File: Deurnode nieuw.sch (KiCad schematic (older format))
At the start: 40 parts, among them J1 EXT1, J10 Jumper Output, J11 Jumper Rel./Fet, J12 Screw_Terminal_01x03, J13 Screw_Terminal_01x03, J14 Screw_Terminal_01x02, J15 Screw_Terminal_01x02, J16 Conn_01x02, J17 Conn_01x02, J18 Barrel_Jack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

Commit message: By means of two jumpers the FET components are isolated from the rest of the board. Current concept version 0.5
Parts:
- removed J13: Screw_Terminal_01x03, TerminalBlock_RND:TerminalBlock_RND_205-00288_1x03_P5.08mm_Horizontal, symbol Connector:Screw_Terminal_01x03
- added J13: Jumper 2 External Power, Connector_PinHeader_2.54mm:PinHeader_1x02_P2.54mm_Vertical, symbol Connector_Generic:Conn_01x02
- added J20: Jumper 1 External Power, Connector_PinHeader_2.54mm:PinHeader_1x03_P2.54mm_Vertical, symbol Connector_Generic:Conn_01x03
- added J21: Screw_Terminal_01x04, TerminalBlock_RND:TerminalBlock_RND_205-00289_1x04_P5.08mm_Horizontal, symbol Connector:Screw_Terminal_01x04
- added OK3: PC814, PC814:DIL04, symbol PC814:PC814
- added R11: 47k, Resistor_THT:R_Axial_DIN0207_L6.3mm_D2.5mm_P7.62mm_Horizontal, symbol Device:R
- R4: value 2k2 -> 4k7
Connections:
- net +12V: now also J20.1 (Pin_1); no longer D2.1 (K)
- net GND: now also J13.1 (Pin_1); no longer D3.1 (K), R5.2, U1.3 (S)
- net at D2.2 (A), R10.1, U1.2 (D): now also J21.3 (Pin_3)
- net at R5.1, U1.1 (G): now also OK3.3 (E); no longer J11.3 (Pin_3)
- net at J10.3 (Pin_3), J11.2 (Pin_2): no longer R4.2
- new net: D2.1 (K), J20.2 (Pin_2), J21.2 (Pin_2), R11.1
- new net: D3.1 (K), J13.2 (Pin_2), J21.4 (Pin_4), R5.2, U1.3 (S)
- new net: J20.3 (Pin_3), J21.1 (Pin_1)
- new net: J11.3 (Pin_3), OK3.1 (AC1)
- new net: OK3.2 (AC2), R4.2
- new net: OK3.4 (C), R11.2
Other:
- note added: "+12V"
- note added: "1A"
- note added: "1B"
- note added: "2A"
- note added: "2B"
- note added: "Coil +"
- note added: "Coil -"
- note added: "Common"
- note added: "Default 230V AC"
- note added: "Ext. gnd"
- note added: "Ext. power +"
- note added: "GND"
- note added: "NC"
- note added: "NO"
- note added: "Schakelaar"
- note removed: "Grote schakelaar"
- moved on the sheet: D1, D2, J10, J11, J12, J4, J5, K1, R2, R5

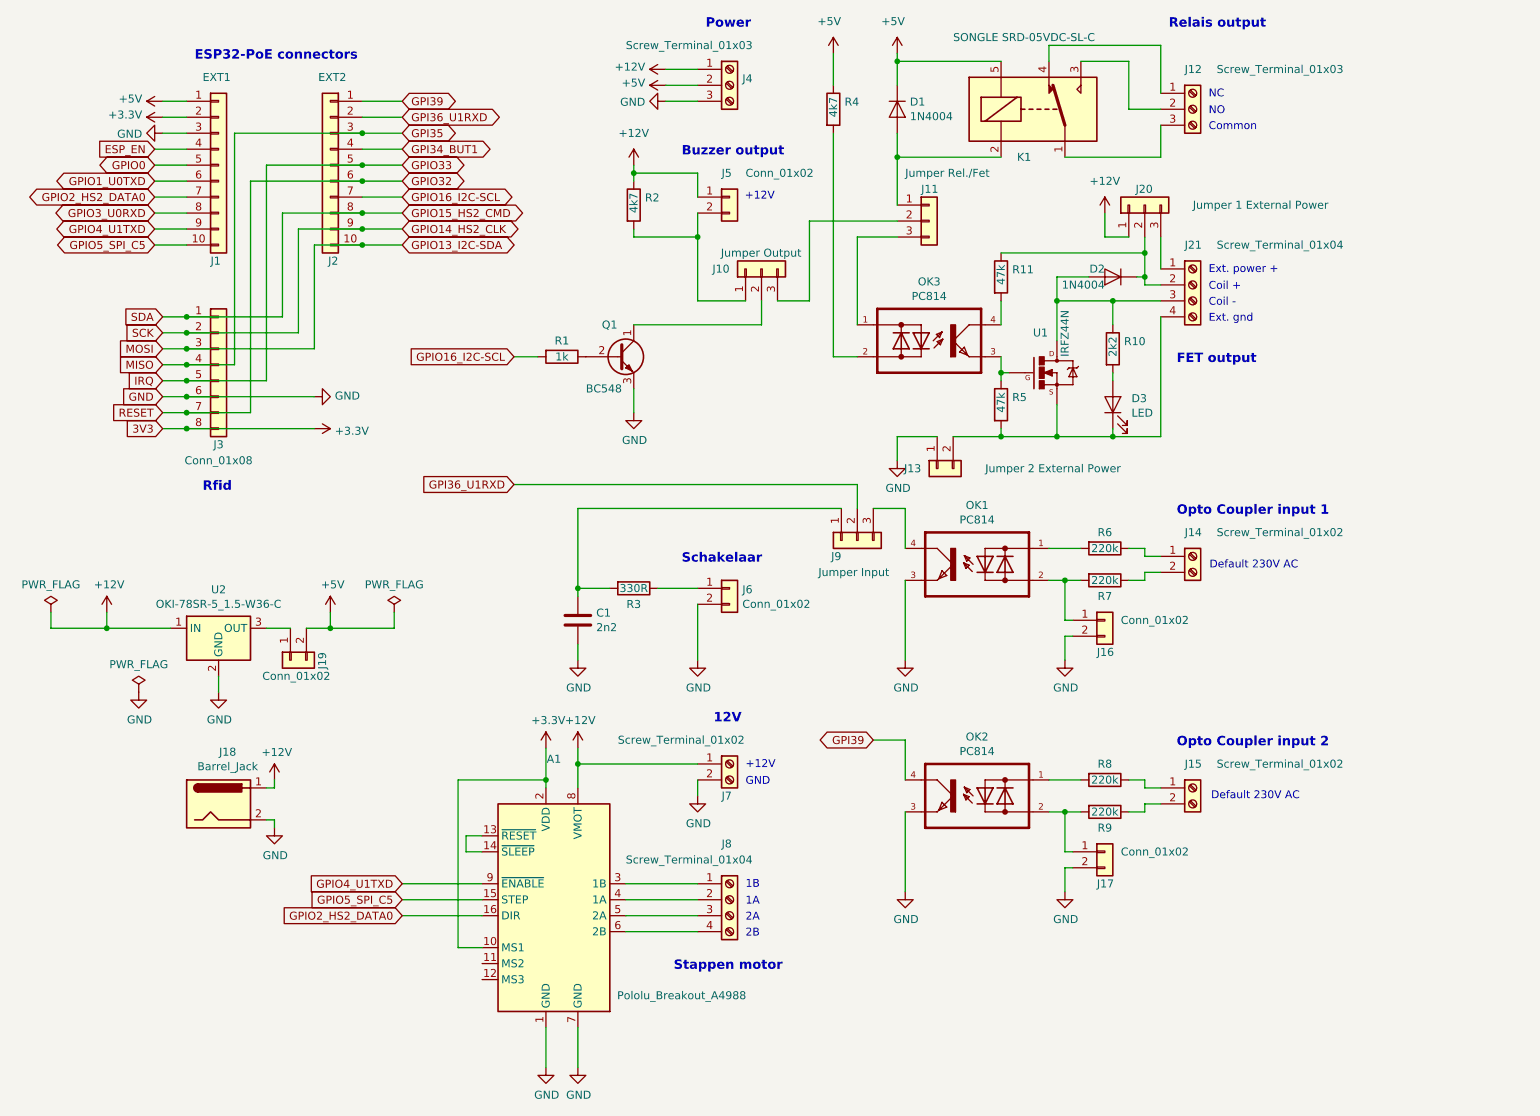
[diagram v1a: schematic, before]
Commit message: Jumper added for Relais/FET override + correct footprint made for 12V barel jack current version concept V0.6
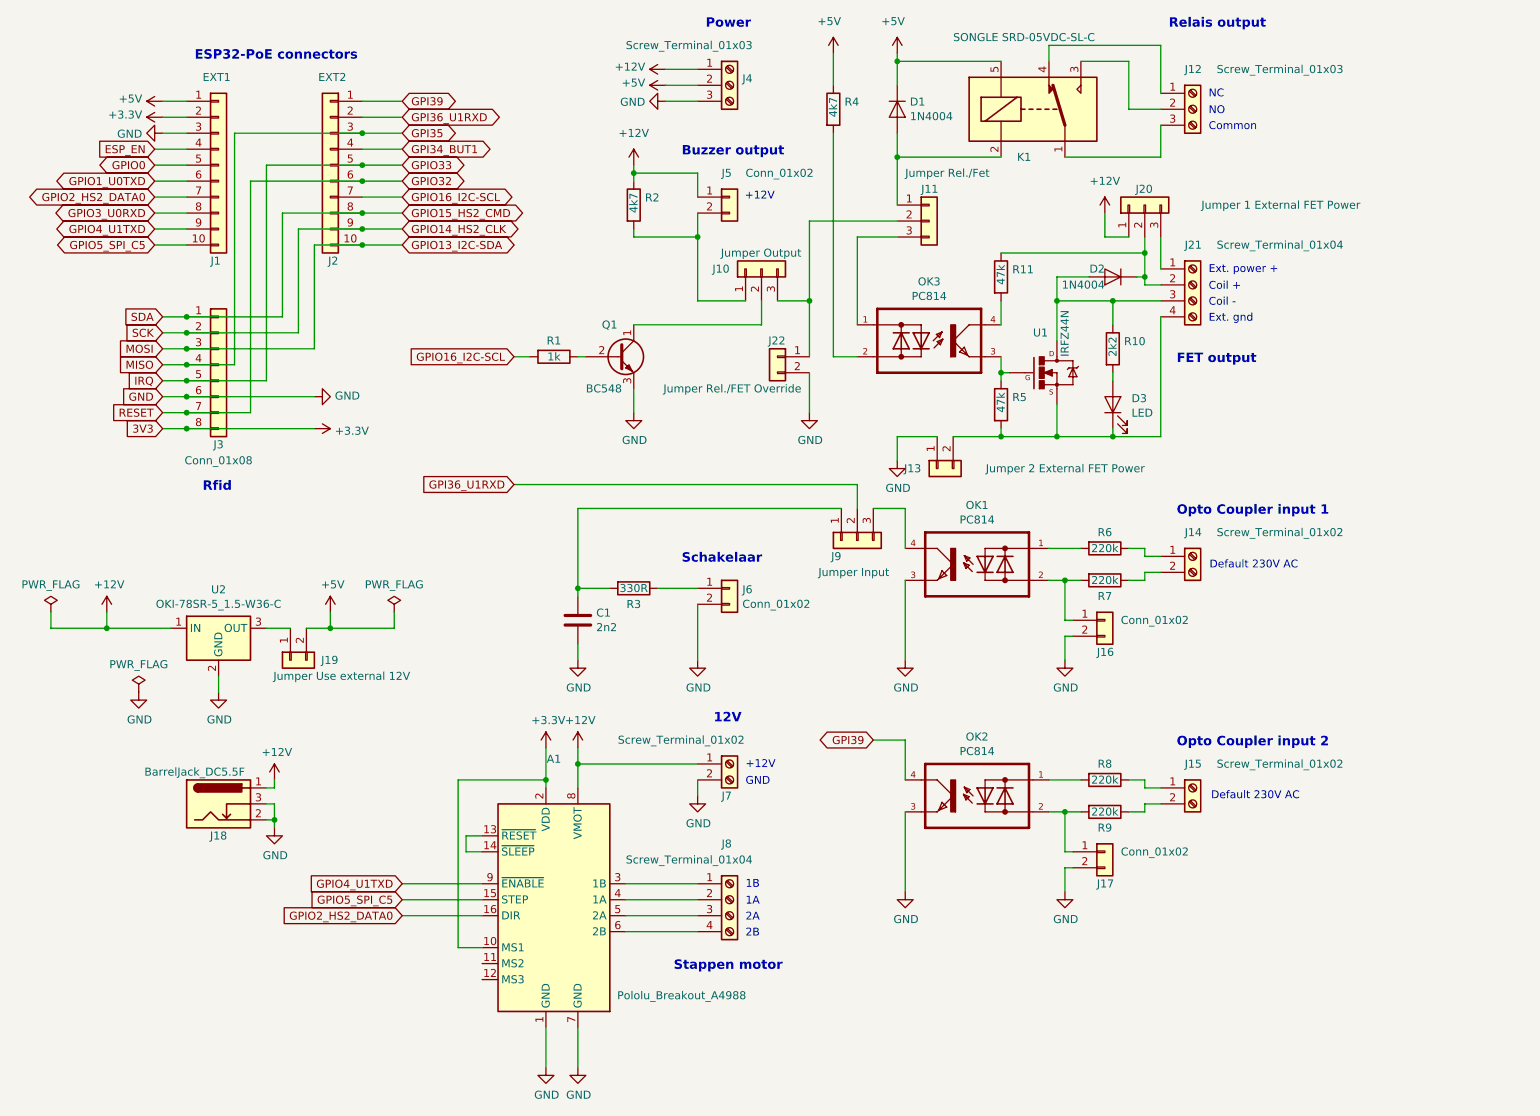
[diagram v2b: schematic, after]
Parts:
- removed J18: Barrel_Jack, Connector_BarrelJack:BarrelJack_CUI_PJ-063AH_Horizontal_CircularHoles, symbol Connector:Barrel_Jack
- added J18: BarrelJack_DC5.5F, Footprints:BarrelJack_DC5.5F, symbol Connector:Barrel_Jack_Switch
- added J22: Jumper Rel./FET Override, Connector_PinHeader_2.54mm:PinHeader_1x02_P2.54mm_Vertical, symbol Connector_Generic:Conn_01x02
- J13: value Jumper 2 External Power -> Jumper 2 External FET Power
- J19: value Conn_01x02 -> Jumper Use external 12V
- J20: value Jumper 1 External Power -> Jumper 1 External FET Power
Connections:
- net +12V: now also J18.1
- net GND: now also J18.2, J18.3, J22.2 (Pin_2)
- net at J10.3 (Pin_3), J11.2 (Pin_2): now also J22.1 (Pin_1)
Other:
- moved on the sheet: R1
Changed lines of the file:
@@
 Sheet 1 1
 Title "Deurnode (based on Olimex ESP32-POE)"
-Date "2020-03-03"
-Rev "Version 0.5"
+Date "2020-03-05"
+Rev "Version 0.6"
 Comp "Makerspace Leiden"
 Comment1 "Hans Beerman"
@@
 L Device:R R1
 U 1 1 5E202795
-P 4650 2700
-F 0 "R1" V 4550 2700 50  0000 C CNN
-F 1 "1k" V 4650 2700 50  0000 C CNN
-F 2 "Resistor_THT:R_Axial_DIN0207_L6.3mm_D2.5mm_P7.62mm_Horizontal" V 4580 2700 50  0001 C CNN
-F 3 "~" H 4650 2700 50  0001 C CNN
-	1    4650 2700
+P 4600 2700
+F 0 "R1" V 4500 2700 50  0000 C CNN
+F 1 "1k" V 4600 2700 50  0000 C CNN
+F 2 "Resistor_THT:R_Axial_DIN0207_L6.3mm_D2.5mm_P7.62mm_Horizontal" V 4530 2700 50  0001 C CNN
+F 3 "~" H 4600 2700 50  0001 C CNN
+	1    4600 2700
 	0    1    1    0
 $EndComp
 Text GLabel 4350 2700 0    50   Input ~ 0
 GPIO16_I2C-SCL
-Wire Wire Line
-	4350 2700 4500 2700
 $Comp
 L Device:R R2
@@
 $EndComp
 $Comp
-L Connector:Barrel_Jack J18
-U 1 1 5E5DAF0A
-P 2500 5500
-F 0 "J18" H 2557 5825 50  0000 C CNN
-F 1 "Barrel_Jack" H 2557 5734 50  0000 C CNN
-F 2 "Connector_BarrelJack:BarrelJack_CUI_PJ-063AH_Horizontal_CircularHoles" H 2550 5460 50  0001 C CNN
-F 3 "~" H 2550 5460 50  0001 C CNN
-	1    2500 5500
-	1    0    0    -1
-$EndComp
-$Comp
 L power:+12V #PWR024
 U 1 1 5E5E3E19
@@
 U 1 1 5E5DCC3F
 P 2950 4600
-F 0 "J19" H 2900 4400 50  0000 L CNN
-F 1 "Conn_01x02" V 3050 4350 50  0000 L CNN
+F 0 "J19" V 2950 4300 50  0000 L CNN
+F 1 "Jumper Use external 12V" V 3050 3850 50  0000 L CNN
 F 2 "Connector_PinHeader_2.54mm:PinHeader_1x02_P2.54mm_Vertical" H 2950 4600 50  0001 C CNN
 F 3 "~" H 2950 4600 50  0001 C CNN
@@
 P 7000 3400
 F 0 "J13" V 7000 3500 50  0000 L CNN
-F 1 "Jumper 2 External Power" V 7000 2250 50  0000 L CNN
+F 1 "Jumper 2 External FET Power" V 7000 2100 50  0000 L CNN
 F 2 "Connector_PinHeader_2.54mm:PinHeader_1x02_P2.54mm_Vertical" H 7000 3400 50  0001 C CNN
 F 3 "~" H 7000 3400 50  0001 C CNN
@@
 P 8300 1750
 F 0 "J20" V 8400 1700 50  0000 L CNN
-F 1 "Jumper 1 External Power" V 8300 600 50  0000 L CNN
+F 1 "Jumper 1 External FET Power" V 8300 400 50  0000 L CNN
 F 2 "Connector_PinHeader_2.54mm:PinHeader_1x03_P2.54mm_Vertical" H 8300 1750 50  0001 C CNN
 F 3 "~" H 8300 1750 50  0001 C CNN
@@
 Wire Wire Line
 	6750 1750 6750 1450
-Wire Wire Line
-	6000 2350 6200 2350
 Wire Wire Line
 	6200 2350 6200 1850
@@
 Text Notes 8715 5480 0    49   ~ 0
 Default 230V AC
+Wire Wire Line
+	4750 2700 4800 2700
+Wire Wire Line
+	4450 2700 4350 2700
+$Comp
+L Connector_Generic:Conn_01x02 J22
+U 1 1 5E6404FC
+P 6000 2700
+F 0 "J22" H 5950 2800 50  0000 L CNN
+F 1 "Jumper Rel./FET Override" H 5850 2500 50  0000 L CNN
+F 2 "Connector_PinHeader_2.54mm:PinHeader_1x02_P2.54mm_Vertical" H 6000 2700 50  0001 C CNN
+F 3 "~" H 6000 2700 50  0001 C CNN
+	1    6000 2700
+	-1   0    0    -1
+$EndComp
+$Comp
+L power:GND #PWR0110
+U 1 1 5E6923E9
+P 6200 3050
+F 0 "#PWR0110" H 6200 2800 50  0001 C CNN
+F 1 "GND" H 6205 2877 50  0000 C CNN
+F 2 "" H 6200 3050 50  0001 C CNN
+F 3 "" H 6200 3050 50  0001 C CNN
+	1    6200 3050
+	1    0    0    -1
+$EndComp
+Wire Wire Line
+	6200 3050 6200 2800
+Wire Wire Line
+	6200 2700 6200 2350
+$Comp
+L Connector:Barrel_Jack_Switch J18
+U 1 1 5E612FDC
+P 2500 5500
+F 0 "J18" H 2500 5300 50  0000 C CNN
+F 1 "BarrelJack_DC5.5F" H 2350 5700 50  0000 C CNN
+F 2 "Footprints:BarrelJack_DC5.5F" H 2550 5460 50  0001 C CNN
+F 3 "~" H 2550 5460 50  0001 C CNN
+	1    2500 5500
+	1    0    0    -1
+$EndComp
+Wire Wire Line
+	2800 5500 2850 5500
+Wire Wire Line
+	2850 5500 2850 5600
+Connection ~ 2850 5600
+Connection ~ 6200 2350
+Wire Wire Line
+	6000 2350 6200 2350
 $EndSCHEMATC

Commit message: removed a lot of jumpers, replaced connectors, added groundplane etc.
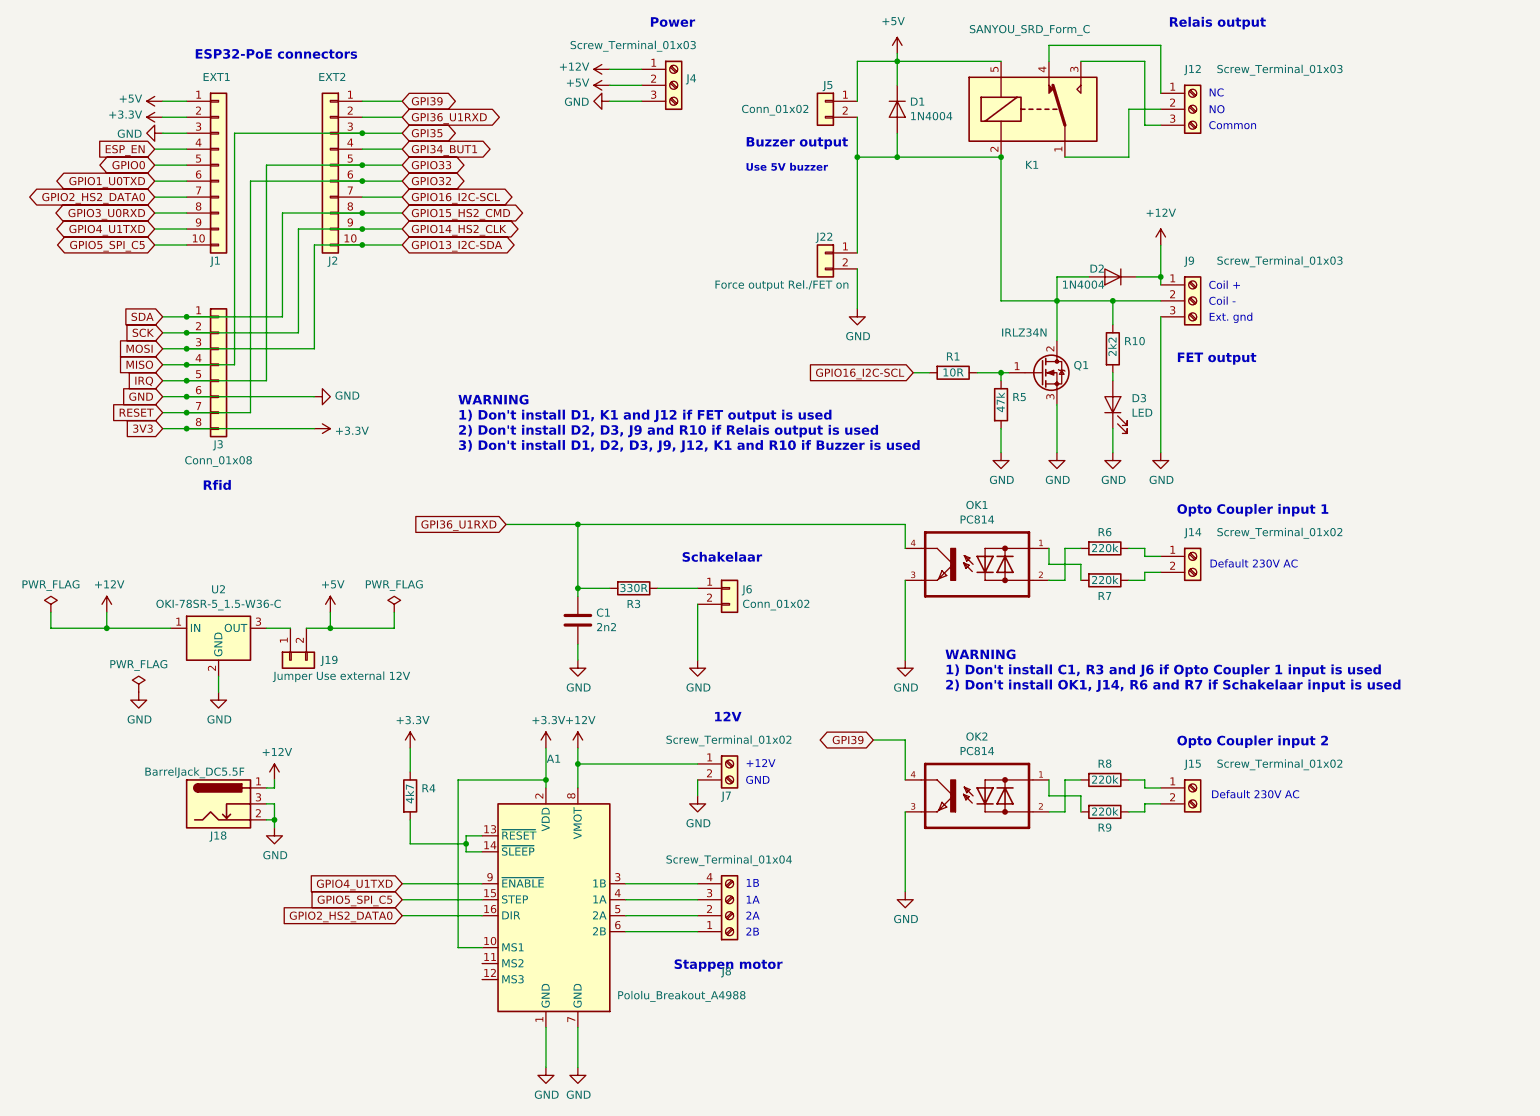
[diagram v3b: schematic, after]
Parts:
- removed J10: Jumper Output, Connector_PinHeader_2.54mm:PinHeader_1x03_P2.54mm_Vertical, symbol Connector_Generic:Conn_01x03
- removed J11: Jumper Rel./Fet, Connector_PinHeader_2.54mm:PinHeader_1x03_P2.54mm_Vertical, symbol Connector_Generic:Conn_01x03
- removed J13: Jumper 2 External FET Power, Connector_PinHeader_2.54mm:PinHeader_1x02_P2.54mm_Vertical, symbol Connector_Generic:Conn_01x02
- removed J16, J17: Conn_01x02, Connector_PinHeader_2.54mm:PinHeader_1x02_P2.54mm_Vertical, symbol Connector_Generic:Conn_01x02
- removed J20: Jumper 1 External FET Power, Connector_PinHeader_2.54mm:PinHeader_1x03_P2.54mm_Vertical, symbol Connector_Generic:Conn_01x03
- removed J21: Screw_Terminal_01x04, TerminalBlock_RND:TerminalBlock_RND_205-00289_1x04_P5.08mm_Horizontal, symbol Connector:Screw_Terminal_01x04
- removed J9: Jumper Input, Connector_PinHeader_2.54mm:PinHeader_1x03_P2.54mm_Vertical, symbol Connector_Generic:Conn_01x03
- removed OK3: PC814, PC814:DIL04, symbol PC814:PC814
- removed Q1: BC548, Package_TO_SOT_THT:TO-92_Inline, symbol Transistor_BJT:BC548
- removed R11: 47k, Resistor_THT:R_Axial_DIN0207_L6.3mm_D2.5mm_P7.62mm_Horizontal, symbol Device:R
- removed R2: 4k7, Resistor_THT:R_Axial_DIN0207_L6.3mm_D2.5mm_P7.62mm_Horizontal, symbol Device:R
- removed U1: IRFZ44N, IRFZ44N:TO-220, symbol IRFZ44N:IRFZ44N
- added J9: Screw_Terminal_01x03, TerminalBlock_RND:TerminalBlock_RND_205-00288_1x03_P5.08mm_Horizontal, symbol Connector:Screw_Terminal_01x03
- added Q1: IRLZ34N, Package_TO_SOT_THT:TO-220-3_Vertical, symbol Transistor_FET:IRLZ34N
- J22: value Jumper Rel./FET Override -> Force output Rel./FET on
- K1: value SONGLE SRD-05VDC-SL-C -> SANYOU_SRD_Form_C
- R1: value 1k -> 10R
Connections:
- net +12V: now also D2.1 (K), J9.1 (Pin_1); no longer J5.1 (Pin_1)
- net +3V3: now also R4.1
- net +5V: now also J5.1 (Pin_1); no longer R4.1
- net GND: now also D3.1 (K), R5.2, J9.3 (Pin_3), Q1.3 (S)
- net GPI36_U1RXD: now also C1.1, OK1.4 (C), R3.2
- net at A1.13 (~RESET), A1.14 (~SLEEP): now also R4.2
- net at A1.3 (1B): now also J8.4 (Pin_4); no longer J8.1 (Pin_1)
- net at A1.4 (1A): now also J8.3 (Pin_3); no longer J8.2 (Pin_2)
- net at A1.5 (2A): now also J8.2 (Pin_2); no longer J8.3 (Pin_3)
- net at A1.6 (2B): now also J8.1 (Pin_1); no longer J8.4 (Pin_4)
- net at J5.2 (Pin_2): now also D1.2 (A), D2.2 (A), J22.1 (Pin_1), K1.2, R10.1, J9.2 (Pin_2), Q1.2 (D)
- net at R1.1: now also R5.1, Q1.1 (G)
- net at K1.1: now also J12.2 (Pin_2); no longer J12.3 (Pin_3)
- net at K1.3: now also J12.3 (Pin_3); no longer J12.2 (Pin_2)
- net at R9.2: now also OK2.1 (AC1); no longer OK2.2 (AC2)
- net at R7.2: now also OK1.1 (AC1); no longer OK1.2 (AC2)
- net at R6.2: now also OK1.2 (AC2); no longer OK1.1 (AC1)
- net at R8.2: now also OK2.2 (AC2); no longer OK2.1 (AC1)
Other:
- note added: "Use 5V buzzer"
- note added: "WARNING\n1) Don't install C1, R3 and J6 if Opto Coupler 1 input is used\n2) Don't install OK1, J14, R6 and R7 if Schakelaar input is used"
- note added: "WARNING\n1) Don't install D1, K1 and J12 if FET output is used\n2) Don't install D2, D3, J9 and R10 if Relais output is used\n3) Don't install D1, D2, D3, J9, J12, K1 and R10 if Buzzer is used"
- note removed: "Ext. power +"
- moved on the sheet: J22, J4, J5, R1
